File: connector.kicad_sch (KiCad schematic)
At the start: 2 parts, among them J1 AXK500137YG, J2 AXK500137YG

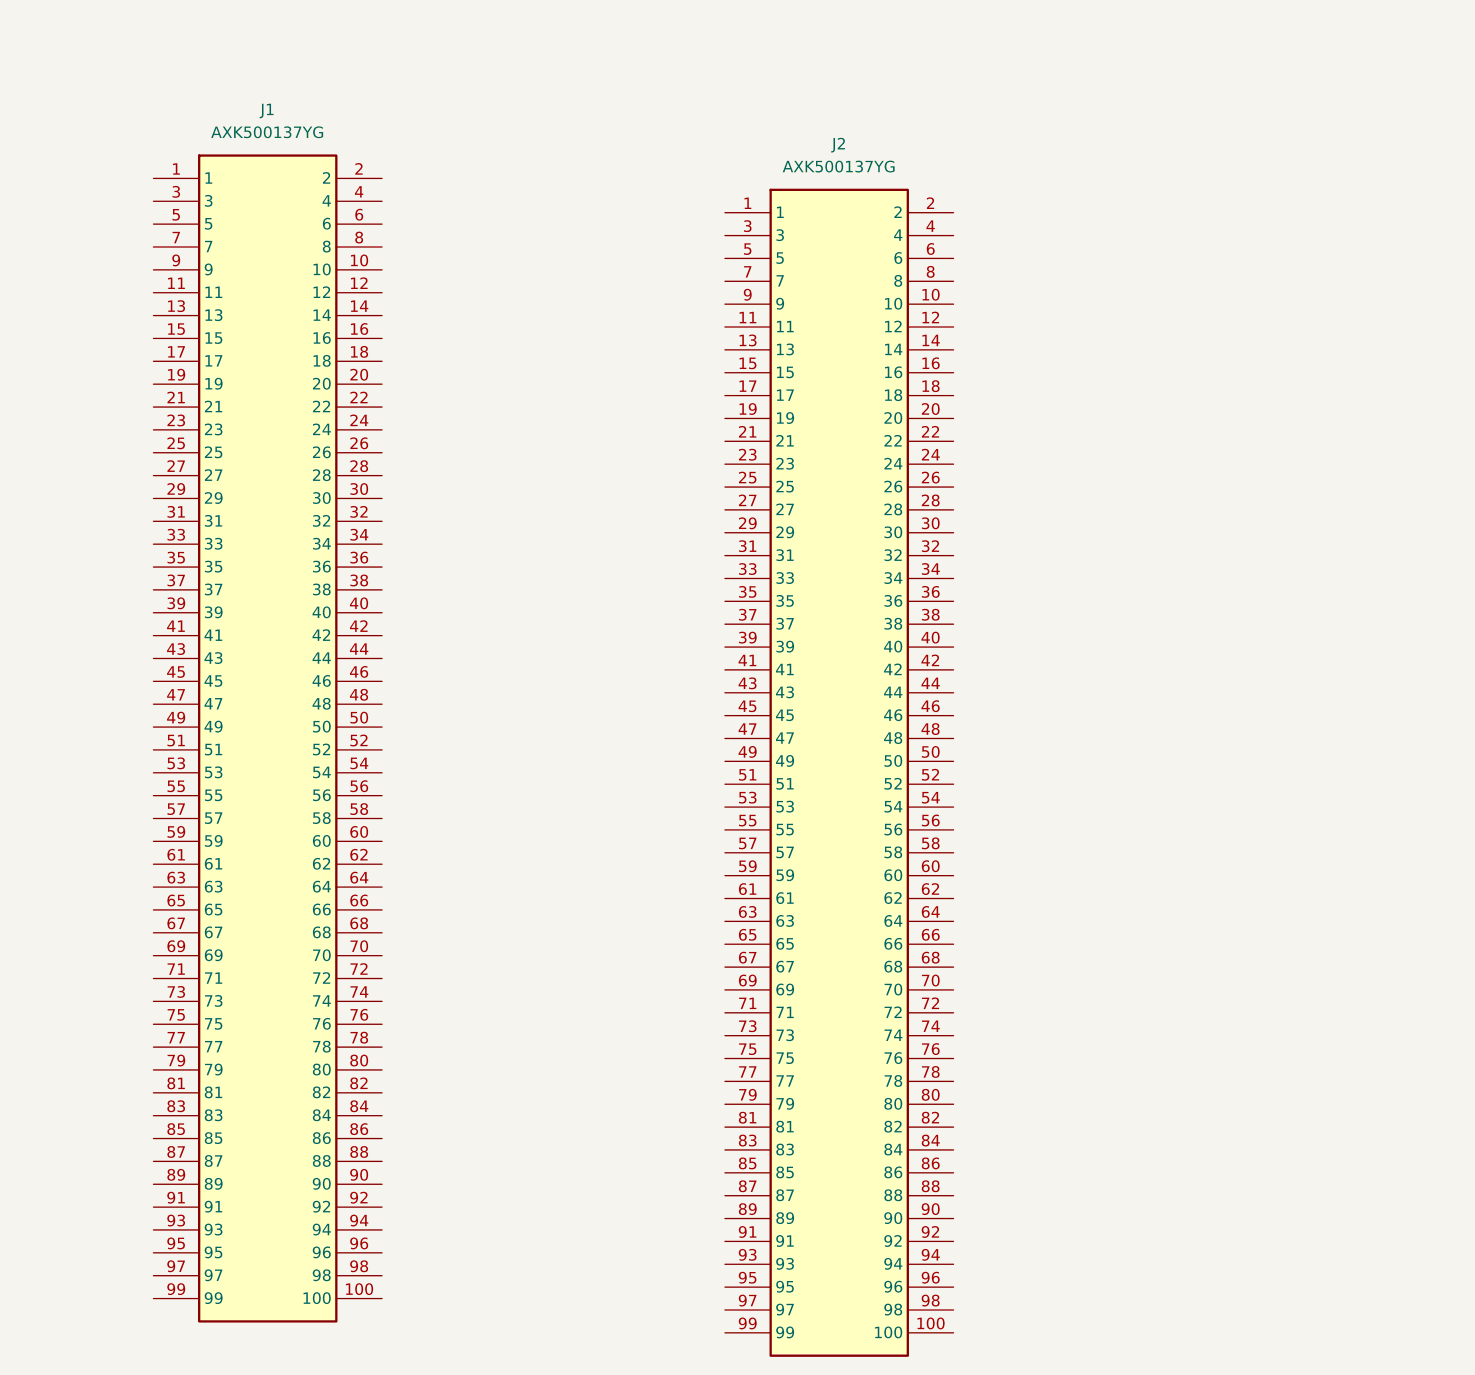
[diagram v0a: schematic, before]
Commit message: feat: finish power sch design
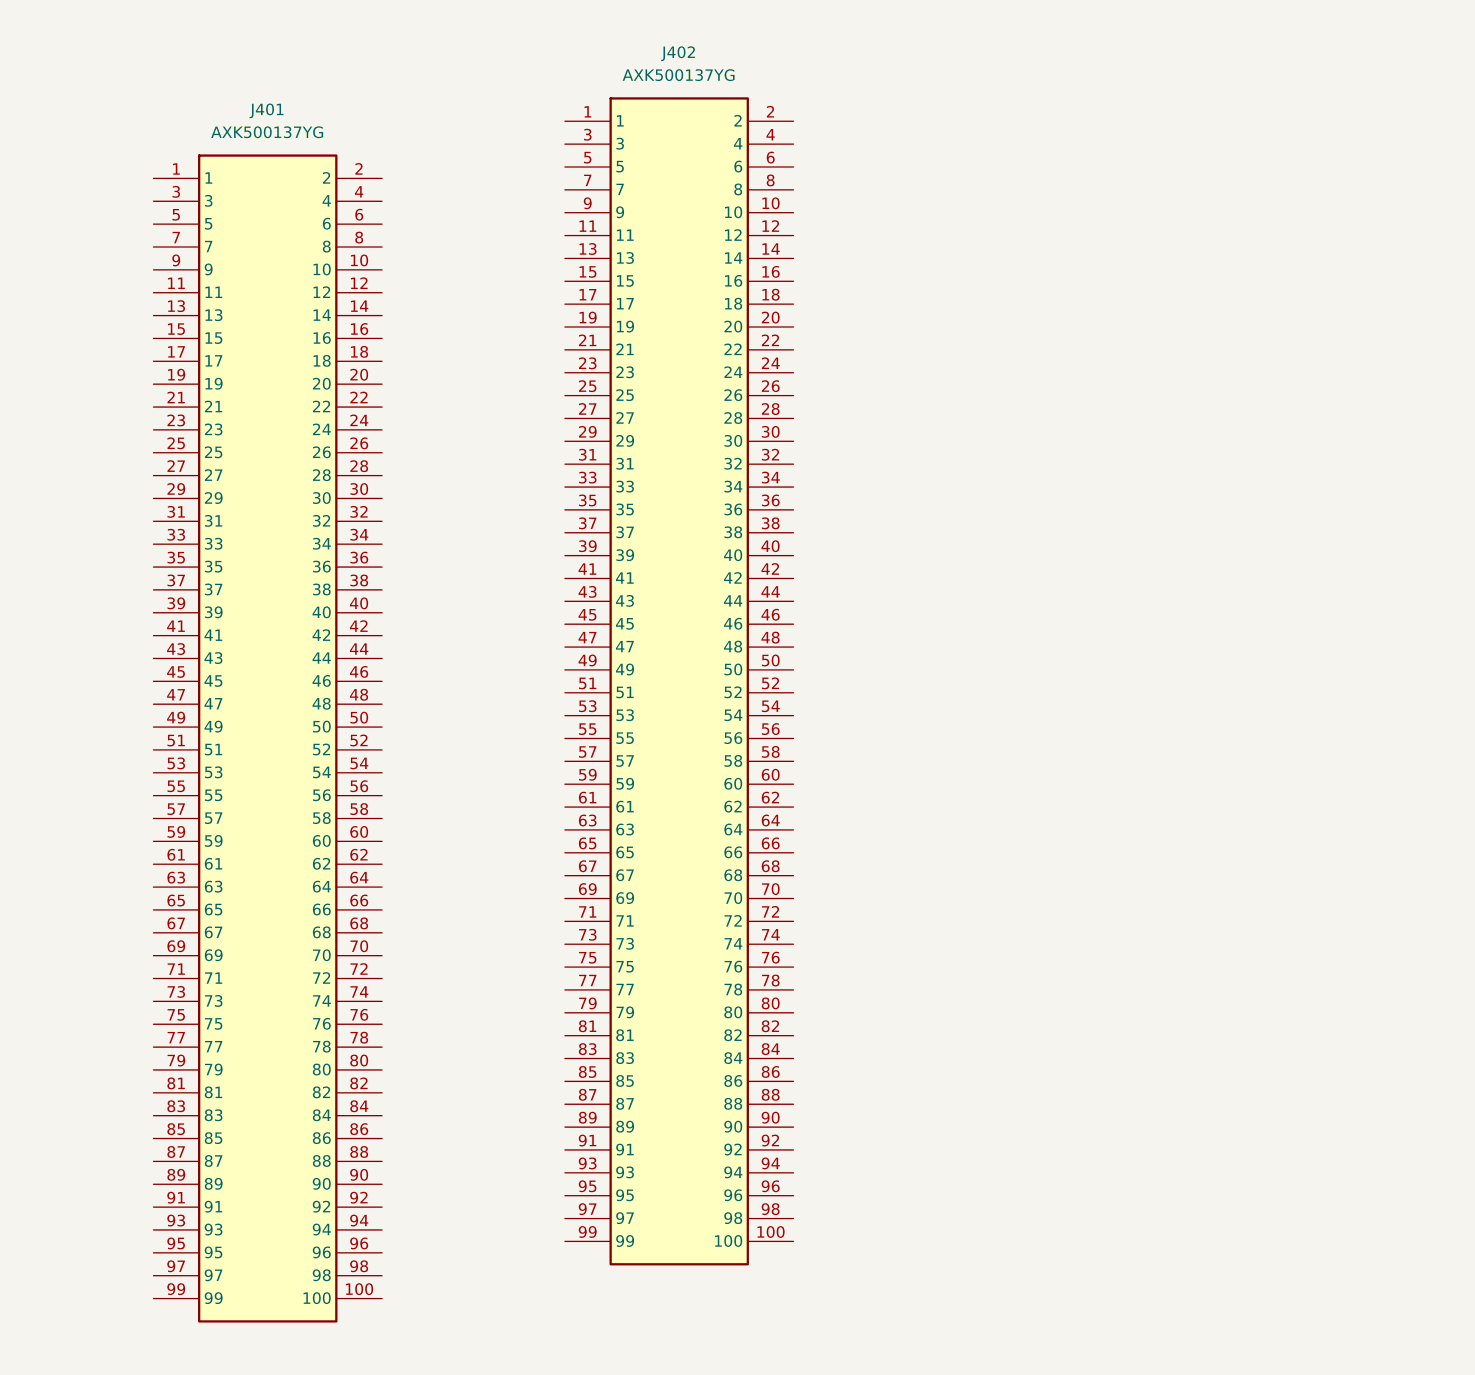
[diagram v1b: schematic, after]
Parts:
- removed J2: AXK500137YG, Project:AXK500137YG, symbol AXK500137YG:AXK500137YG
- added J402: AXK500137YG, Project:AXK500137YG, symbol AXK500137YG:AXK500137YG
- renumbered J1 to J401

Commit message: feat: continue improve sch design
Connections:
- net +VCCIO_35: now reaches J402.1
- net +VCCIO_35: now also J402.2, J402.3, J402.4
- net +VCCIO_34: now reaches J401.1
- net +VCCIO_34: now also J401.2, J401.3, J401.4
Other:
- moved on the sheet: J402

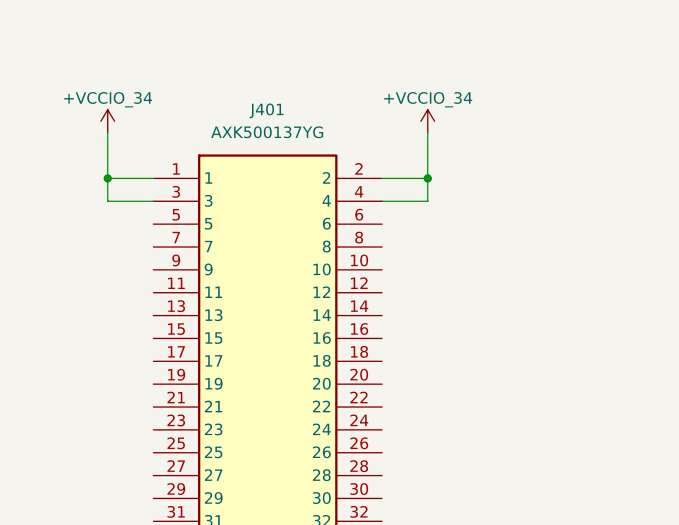
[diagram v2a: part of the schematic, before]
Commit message: feat: finish basic ddr3 routing
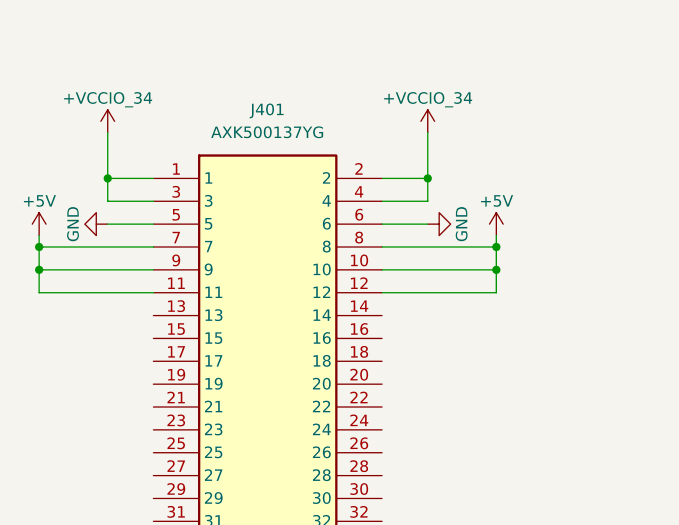
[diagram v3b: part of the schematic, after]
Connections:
- net +5V: now reaches J401.10
- net +5V: now also J401.11, J401.12, J401.7, J401.8, J401.9
- net GND: now reaches J401.5
- net GND: now also J401.6

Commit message: feat: need finish power layout
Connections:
- net PL_B34_IO8_N: now reaches J401.86
- net PL_B34_IO8_P: now reaches J401.88
- net PL_B34_IO4_N: now reaches J401.92
- net PL_B34_IO4_P: now reaches J401.94
- net PL_B34_IO1_P: now reaches J401.96
- net PL_B34_IO1_N: now reaches J401.98
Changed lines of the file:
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@@
+		)
+	)
+	(global_label "PL_B34_IO4_N"
+		(shape bidirectional)
+		(at 90.17 160.02 0)
+		(effects
+			(font
+				(size 1.27 1.27)
+			)
+			(justify left)
+		)
+		(property "Intersheetrefs" "${INTERSHEET_REFS}"
+			(at 90.17 160.02 0)
+			(hide yes)
+			(show_name no)
+			(do_not_autoplace no)
+			(effects
+				(font
+					(size 1.27 1.27)
+				)
+			)
+		)
+	)
+	(global_label "PL_B34_IO1_P"
+		(shape bidirectional)
+		(at 90.17 165.1 0)
+		(effects
+			(font
+				(size 1.27 1.27)
+			)
+			(justify left)
+		)
+		(property "Intersheetrefs" "${INTERSHEET_REFS}"
+			(at 90.17 165.1 0)
+			(hide yes)
+			(show_name no)
+			(do_not_autoplace no)
+			(effects
+				(font
+					(size 1.27 1.27)
+				)
+			)
+		)
+	)
+	(global_label "PL_B34_IO1_N"
+		(shape bidirectional)
+		(at 90.17 167.64 0)
+		(effects
+			(font
+				(size 1.27 1.27)
+			)
+			(justify left)
+		)
+		(property "Intersheetrefs" "${INTERSHEET_REFS}"
+			(at 90.17 167.64 0)
+			(hide yes)
+			(show_name no)
+			(do_not_autoplace no)
+			(effects
+				(font
+					(size 1.27 1.27)
+				)
+			)
+		)
+	)
+	(global_label "PL_B34_IO4_P"
+		(shape bidirectional)
+		(at 90.17 162.56 0)
+		(effects
+			(font
+				(size 1.27 1.27)
+			)
+			(justify left)
+		)
+		(property "Intersheetrefs" "${INTERSHEET_REFS}"
+			(at 90.17 162.56 0)
+			(hide yes)
+			(show_name no)
+			(do_not_autoplace no)
+			(effects
+				(font
+					(size 1.27 1.27)
+				)
+			)
+		)
+	)
+	(global_label "PL_B34_IO8_P"
+		(shape bidirectional)
+		(at 90.17 154.94 0)
+		(effects
+			(font
+				(size 1.27 1.27)
+			)
+			(justify left)
+		)
+		(property "Intersheetrefs" "${INTERSHEET_REFS}"
+			(at 90.17 154.94 0)
+			(hide yes)
+			(show_name no)
+			(do_not_autoplace no)
+			(effects
+				(font
+					(size 1.27 1.27)
+				)
+			)
+		)
+	)
+	(global_label "PL_B34_IO8_N"
+		(shape bidirectional)
+		(at 90.17 152.4 0)
+		(effects
+			(font
+				(size 1.27 1.27)
+			)
+			(justify left)
+		)
+		(property "Intersheetrefs" "${INTERSHEET_REFS}"
+			(at 90.17 152.4 0)
+			(hide yes)
+			(show_name no)
+			(do_not_autoplace no)
+			(effects
+				(font
+					(size 1.27 1.27)
+				)
+			)
 		)
 	)
